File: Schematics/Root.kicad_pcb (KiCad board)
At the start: 2 copper layers, 50 x 50 mm, 52 parts, among them CON1 USB-MICRO-B, CON2 BARREL_JACK, IC1 ATXMEGA256A3BU-A, J1 AVR_JTAG_Header, P1 CONN_01X06, P10 CONN_01X06, P11 CONN_01X06, P12 CONN_01X06, P2 CONN_01X06, P3 CONN_01X06, P4 CONN_01X06, P5 CONN_01X06, P6 CONN_01X06, P7 CONN_01X06, P8 CONN_01X06, P9 CONN_01X06, SW1 SW_PUSH, SW2 SW_PUSH, U13 LT8612, X1 16MHz, X2 32.768KhZ

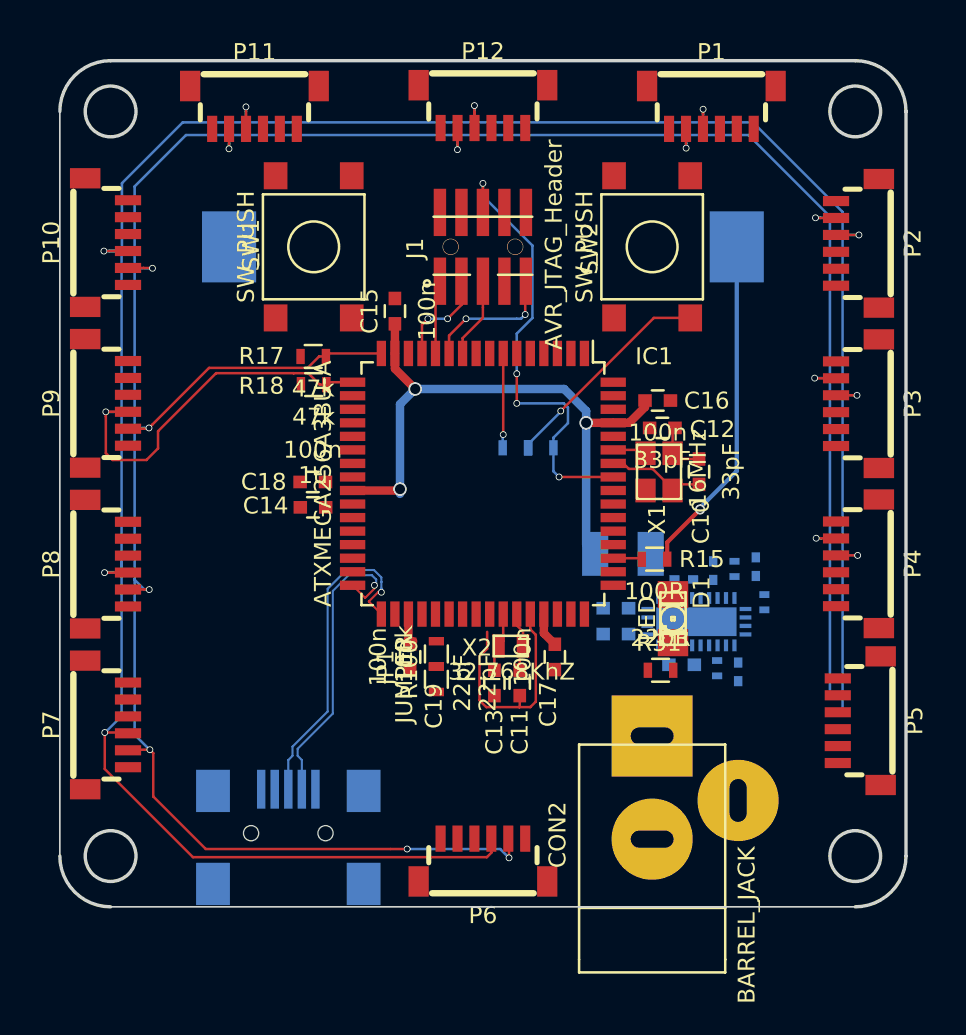
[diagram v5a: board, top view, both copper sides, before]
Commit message: Split design into two modules
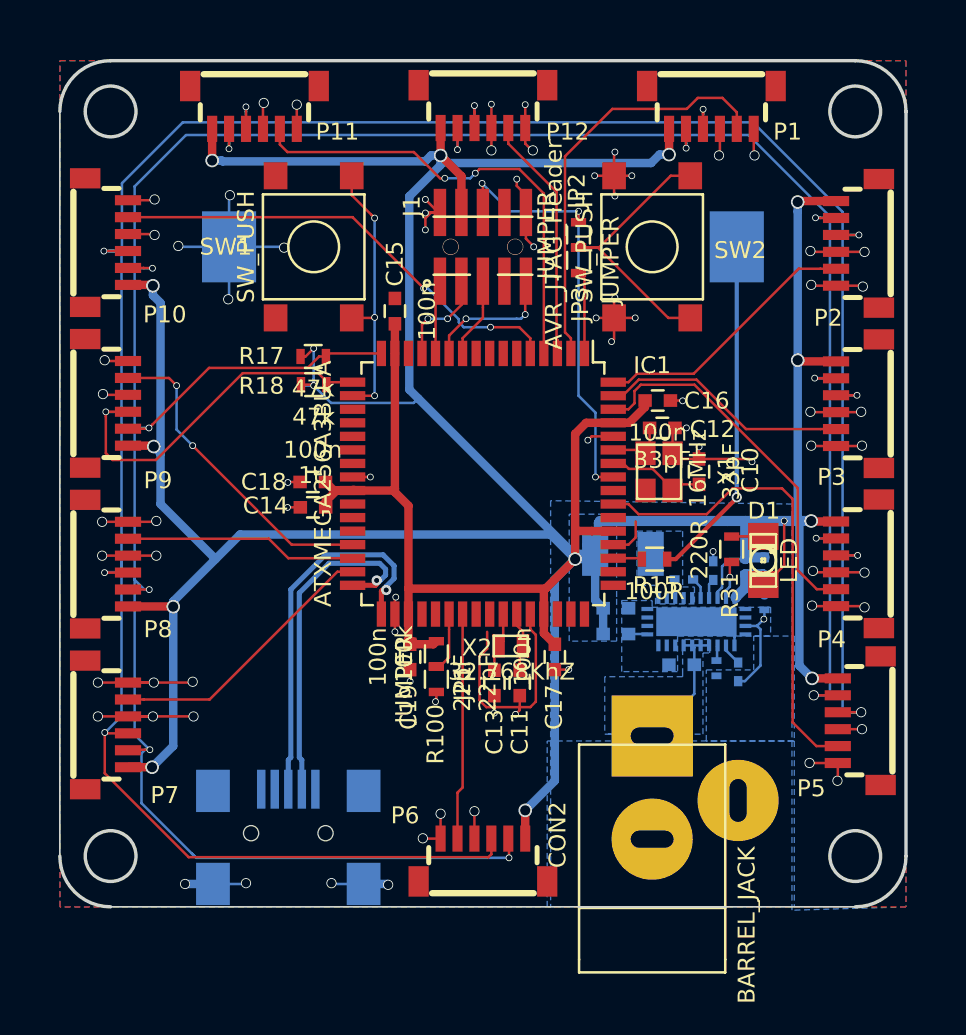
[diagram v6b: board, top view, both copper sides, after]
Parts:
- JP2, JP3: moved to F.Cu
- moved JP2 12.8 mm to (80.7, 160.3), turned to 270 degrees
- moved JP3 11.7 mm to (80.7, 161.8), turned to 90 degrees
- moved R31 8.30 mm to (89.7, 178.9), turned to 270 degrees
- moved D1 6.35 mm to (91.6, 179.5), turned to 90 degrees
- moved R33 0.65 mm to (90.5, 179.9)
- moved C37 0.53 mm to (91.7, 179.9)
- turned R32 to 270 degrees
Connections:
- IC1 pad 1: (no net) -> /Microcontroller/SW2
- IC1 pad 18: (no net) -> /Microcontroller/SW1
- IC1 pad 2: (no net) -> /~OE1
- IC1 pad 26: /~OE1 -> (no net)
- IC1 pad 27: /~OE2 -> (no net)
- IC1 pad 28: /~OE3 -> (no net)
- IC1 pad 29: /~OE4 -> /~OE9
- IC1 pad 3: (no net) -> /~OE12
- IC1 pad 30: /~OE5 -> /~OE8
- IC1 pad 31: /~OE6 -> /~OE7
- IC1 pad 38: (no net) -> /Microcontroller/JUMPER
- IC1 pad 39: (no net) -> /~OE6
- IC1 pad 4: (no net) -> /~OE11
- IC1 pad 41: /Microcontroller/JUMPER -> (no net)
- IC1 pad 48: /~OE7 -> (no net)
- IC1 pad 49: /~OE8 -> (no net)
- IC1 pad 5: (no net) -> /~OE10
- IC1 pad 50: /~OE9 -> (no net)
- IC1 pad 55: (no net) -> /~OE5
- IC1 pad 6: /Microcontroller/SW1 -> (no net)
- IC1 pad 62: /~OE10 -> /~OE4
- IC1 pad 63: /~OE11 -> /~OE3
- IC1 pad 64: /~OE12 -> /~OE2
- IC1 pad 7: /Microcontroller/SW2 -> (no net)
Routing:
- net VPP: track 41.4 -> 286.9 mm, vias 3 -> 16
- net GND: track 17.9 -> 149.6 mm, vias 0 -> 78
- net /~OE5: track 0.00 -> 28.7 mm
- net /~OE10: track 0.00 -> 27.7 mm, vias 0 -> 2
- net /~OE11: track 0.00 -> 27.6 mm, vias 0 -> 2
- net /~OE1: track 0.00 -> 24.7 mm
- net /~OE4: track 0.00 -> 22.0 mm
- net /~OE9: track 0.00 -> 18.9 mm, vias 0 -> 2
- net /~OE7: track 0.00 -> 16.4 mm
- net /Microcontroller/SW1: track 0.00 -> 16.2 mm, vias 0 -> 3
- net /~OE2: track 0.00 -> 15.9 mm
- net /~OE3: track 0.00 -> 14.8 mm
- net /~OE12: track 0.00 -> 14.5 mm
- net /~OE8: track 0.00 -> 13.7 mm
- net /~OE6: track 0.00 -> 13.4 mm
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- added copper zone on B.Cu, net /Power Supply/SW
- added copper zone on B.Cu, net /Power Supply/Vin
- added copper zone on B.Cu, net GND
- added copper zone on F.Cu, net GND
- added copper zone on B.Cu, net VPP

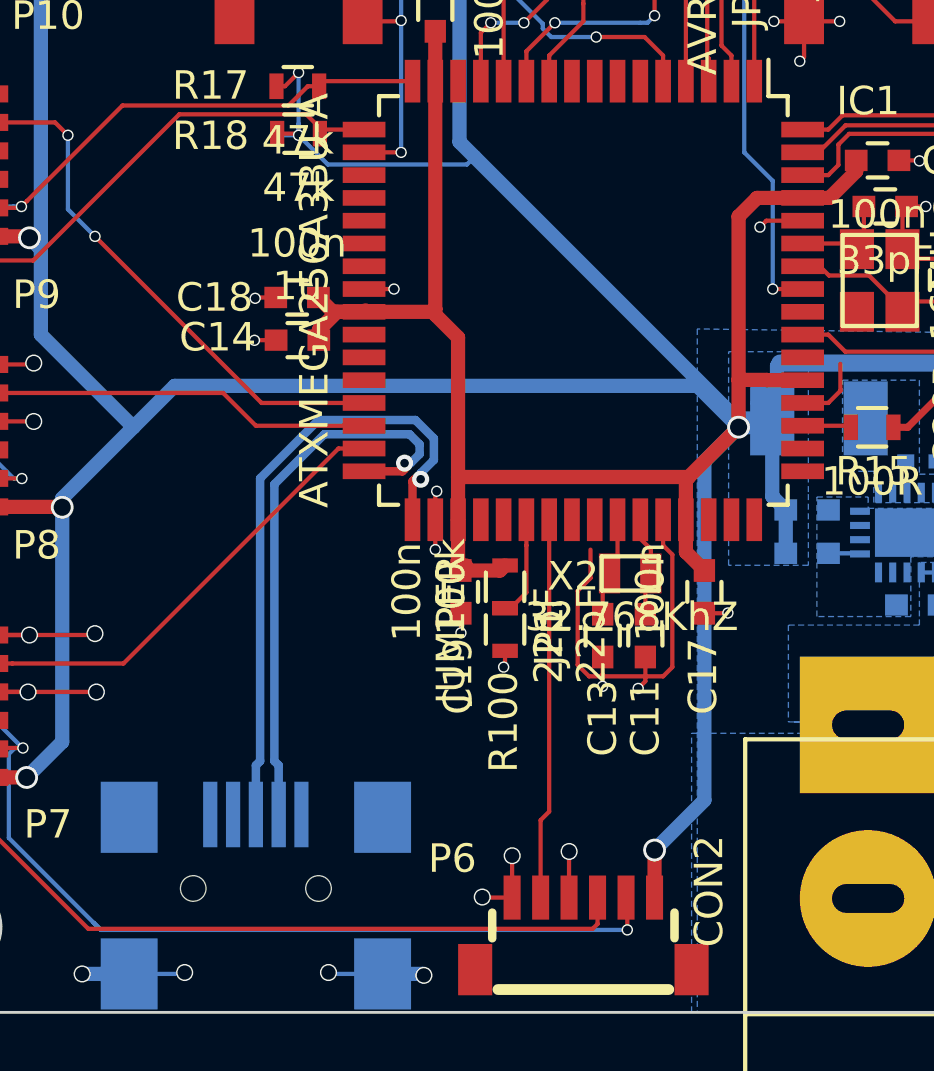
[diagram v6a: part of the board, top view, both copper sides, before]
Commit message: Added some debug headers for power and UART
Added silkscreen info also.
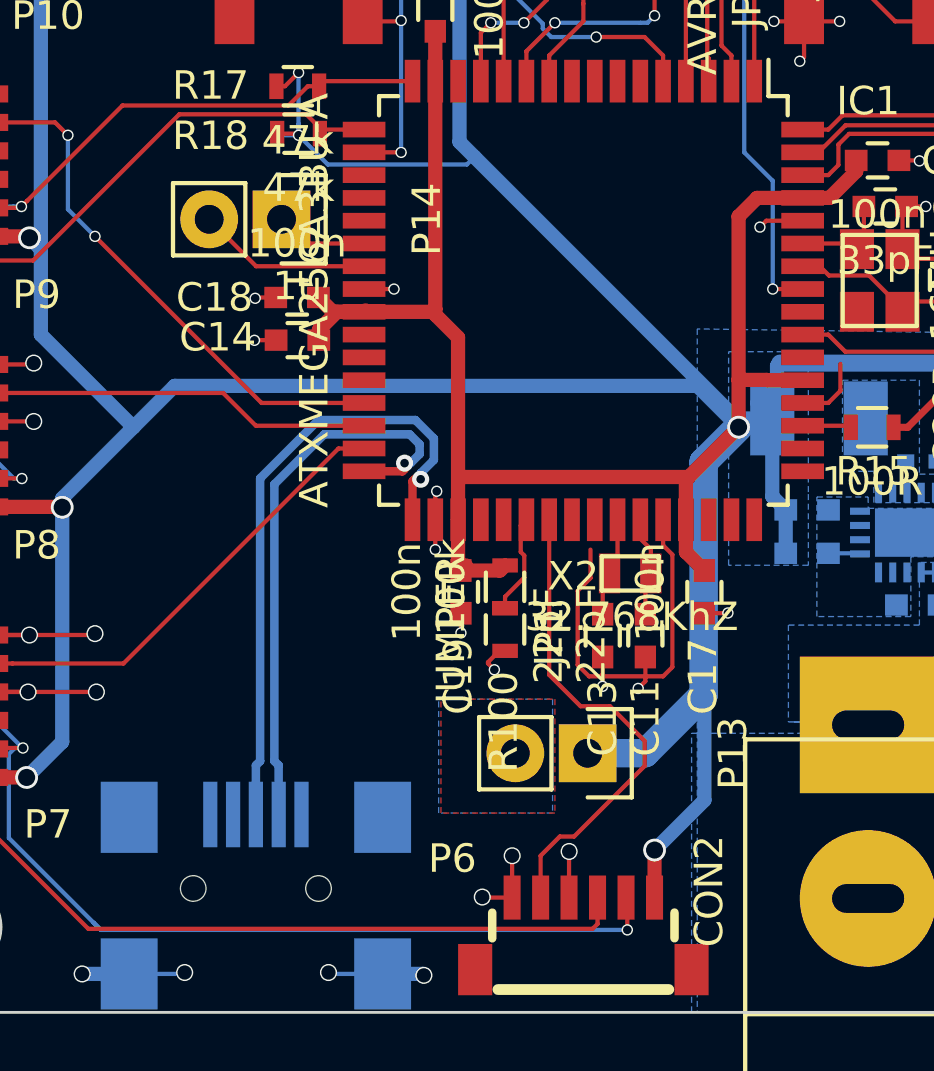
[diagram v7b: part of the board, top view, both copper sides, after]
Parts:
- added P13: CONN_01X02, Pin_Headers:Pin_Header_Straight_1x02, F.Cu at (75.2, 190.9)
- added P14: CONN_01X02, Pin_Headers:Pin_Header_Straight_1x02, F.Cu at (64.4, 172.2)
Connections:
- IC1 pad 22: (no net) -> /Microcontroller/AVR_RXD
- IC1 pad 23: (no net) -> /Microcontroller/AVR_TXD
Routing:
- net VPP: track 286.9 -> 301.8 mm
- net /Microcontroller/AVR_TXD: track 0.00 -> 6.12 mm
- net /~OE6: track 13.4 -> 17.1 mm
- net /Microcontroller/AVR_RXD: track 0.00 -> 3.25 mm
- net GND: track 149.6 -> 150.2 mm
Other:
- board text added: "RGB Clock Root PCB github/seblovett/RGB_Clock V1.0"
